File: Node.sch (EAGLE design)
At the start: 53 parts, among them J2 DF12A3.0-14DS, Q1 16MHz, U1 ATMEGA32U4QFN, U2 NRF24L01SMD, U3 LTC3553, U4 L3GD20, U6 LSM303DLHC, U9 RCLAMP0502A, X1 USBSMD

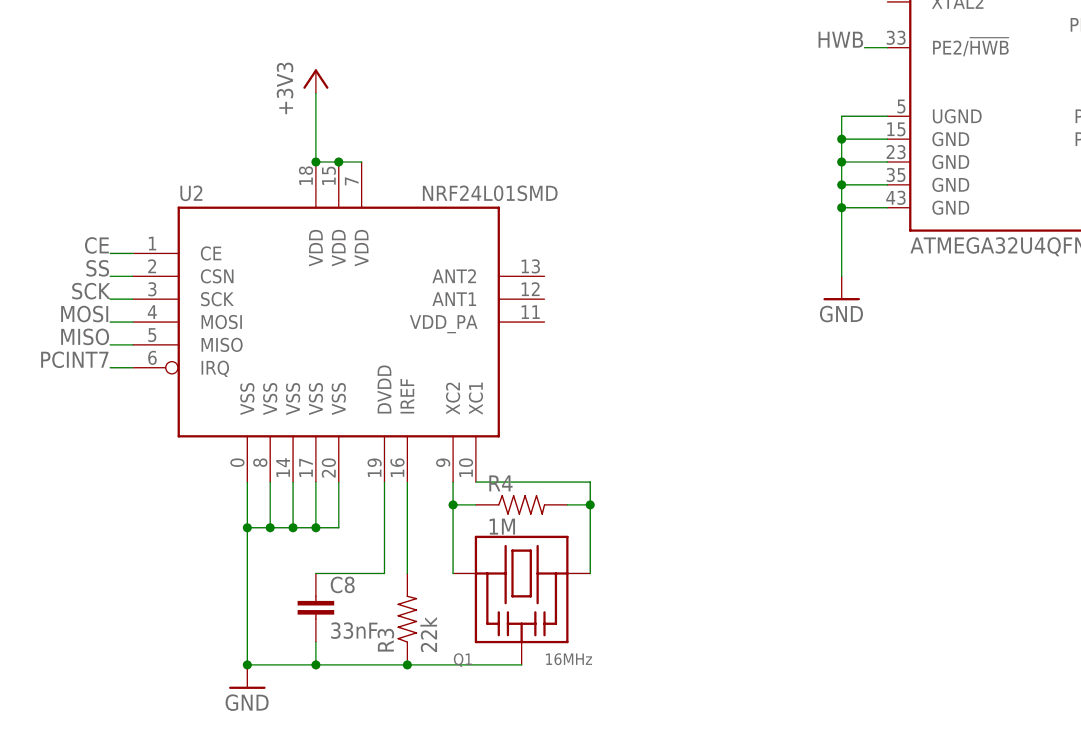
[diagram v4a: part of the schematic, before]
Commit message: balun for nrf24l01
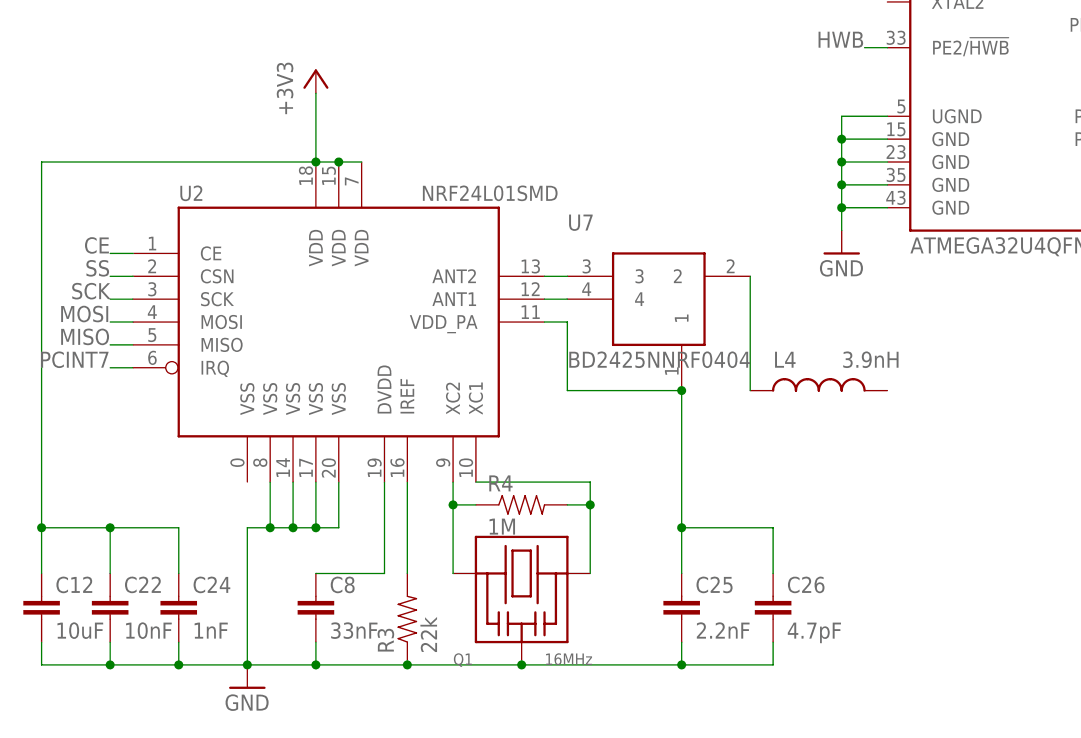
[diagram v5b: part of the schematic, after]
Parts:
- added C12: 10uF, SparkFun:CAP0603-CAP
- added C22: 10nF, SparkFun:CAP0402-CAP
- added C24: 1nF, SparkFun:CAP0402-CAP
- added C25: 2.2nF, SparkFun:CAP0402-CAP
- added C26: 4.7pF, SparkFun:CAP0402-CAP
- added L4: 3.9nH, adjacent-reality:INDUCTOR0402
- added U7: BD2425NNRF0404, adjacent-reality:BD2425NNRF0404
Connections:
- new net N$21: U2.ANT2, U7.3
- new net N$22: U2.ANT1, U7.4
- new net N$23: C25.1, C26.1, U2.VDD_PA, U7.1
- new net N$28: L4.1, U7.2
- net +3V3: now also C12.1, C22.1, C24.1
- net GND: now also C12.2, C22.2, C24.2, C25.2, C26.2; no longer U2.VSS@0
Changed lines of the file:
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@@
 <part name="GND9" library="supply1" deviceset="GND" device=""/>
 <part name="+3V8" library="supply1" deviceset="+3V3" device=""/>
+<part name="C12" library="SparkFun" deviceset="CAP" device="0603-CAP" value="10uF"/>
+<part name="C22" library="SparkFun" deviceset="CAP" device="0402-CAP" value="10nF"/>
+<part name="C24" library="SparkFun" deviceset="CAP" device="0402-CAP" value="1nF"/>
+<part name="C25" library="SparkFun" deviceset="CAP" device="0402-CAP" value="2.2nF"/>
+<part name="C26" library="SparkFun" deviceset="CAP" device="0402-CAP" value="4.7pF"/>
+<part name="L4" library="adjacent-reality" deviceset="INDUCTOR" device="0402" value="3.9nH"/>
+<part name="U7" library="adjacent-reality" deviceset="BD2425NNRF" device="0404"/>
 </parts>
 <sheets>
@@
 <instance part="C7" gate="G$1" x="195.58" y="132.08"/>
 <instance part="GND2" gate="1" x="208.28" y="109.22"/>
-<instance part="GND3" gate="1" x="99.06" y="50.8"/>
+<instance part="GND3" gate="1" x="99.06" y="55.88"/>
 <instance part="+3V3" gate="G$1" x="99.06" y="152.4"/>
 <instance part="X1" gate="G$1" x="20.32" y="187.96" rot="R180"/>
@@
 <instance part="GND9" gate="1" x="185.42" y="121.92"/>
 <instance part="+3V8" gate="G$1" x="185.42" y="149.86"/>
+<instance part="C12" gate="G$1" x="10.16" y="15.24"/>
+<instance part="C22" gate="G$1" x="17.78" y="15.24"/>
+<instance part="C24" gate="G$1" x="25.4" y="15.24"/>
+<instance part="C25" gate="G$1" x="81.28" y="15.24"/>
+<instance part="C26" gate="G$1" x="91.44" y="15.24"/>
+<instance part="L4" gate="G$1" x="96.52" y="40.64" smashed="yes" rot="R90">
+<attribute name="NAME" x="91.44" y="43.18" size="1.778" layer="95"/>
+<attribute name="VALUE" x="99.06" y="43.18" size="1.778" layer="96"/>
+</instance>
+<instance part="U7" gate="G$1" x="78.74" y="50.8"/>
 </instances>
 <busses>
@@
 <wire x1="99.06" y1="60.96" x2="99.06" y2="63.5" width="0.1524" layer="91"/>
 <junction x="99.06" y="63.5"/>
-<wire x1="99.06" y1="60.96" x2="99.06" y2="53.34" width="0.1524" layer="91"/>
+<wire x1="99.06" y1="60.96" x2="99.06" y2="58.42" width="0.1524" layer="91"/>
 <junction x="99.06" y="60.96"/>
 <pinref part="GND3" gate="1" pin="GND"/>
@@
 </segment>
 <segment>
-<pinref part="U2" gate="G$1" pin="VSS@0"/>
 <pinref part="GND4" gate="1" pin="GND"/>
-<wire x1="33.02" y1="30.48" x2="33.02" y2="25.4" width="0.1524" layer="91"/>
 <pinref part="U2" gate="G$1" pin="VSS@8"/>
 <wire x1="33.02" y1="25.4" x2="33.02" y2="10.16" width="0.1524" layer="91"/>
 <wire x1="33.02" y1="25.4" x2="35.56" y2="25.4" width="0.1524" layer="91"/>
 <wire x1="35.56" y1="25.4" x2="35.56" y2="30.48" width="0.1524" layer="91"/>
-<junction x="33.02" y="25.4"/>
 <pinref part="U2" gate="G$1" pin="VSS@14"/>
 <wire x1="35.56" y1="25.4" x2="38.1" y2="25.4" width="0.1524" layer="91"/>
@@
 <wire x1="63.5" y1="10.16" x2="50.8" y2="10.16" width="0.1524" layer="91"/>
 <junction x="50.8" y="10.16"/>
+<pinref part="C12" gate="G$1" pin="2"/>
+<wire x1="10.16" y1="12.7" x2="10.16" y2="10.16" width="0.1524" layer="91"/>
+<wire x1="10.16" y1="10.16" x2="17.78" y2="10.16" width="0.1524" layer="91"/>
+<pinref part="C22" gate="G$1" pin="2"/>
+<wire x1="17.78" y1="10.16" x2="25.4" y2="10.16" width="0.1524" layer="91"/>
+<wire x1="25.4" y1="10.16" x2="33.02" y2="10.16" width="0.1524" layer="91"/>
+<wire x1="17.78" y1="12.7" x2="17.78" y2="10.16" width="0.1524" layer="91"/>
+<junction x="17.78" y="10.16"/>
+<pinref part="C24" gate="G$1" pin="2"/>
+<wire x1="25.4" y1="12.7" x2="25.4" y2="10.16" width="0.1524" layer="91"/>
+<junction x="25.4" y="10.16"/>
+<junction x="63.5" y="10.16"/>
+<pinref part="C25" gate="G$1" pin="2"/>
+<wire x1="81.28" y1="10.16" x2="63.5" y2="10.16" width="0.1524" layer="91"/>
+<wire x1="81.28" y1="12.7" x2="81.28" y2="10.16" width="0.1524" layer="91"/>
+<junction x="81.28" y="10.16"/>
+<pinref part="C26" gate="G$1" pin="2"/>
+<wire x1="91.44" y1="10.16" x2="81.28" y2="10.16" width="0.1524" layer="91"/>
+<wire x1="91.44" y1="12.7" x2="91.44" y2="10.16" width="0.1524" layer="91"/>
 </segment>
 <segment>
@@
 <wire x1="43.18" y1="66.04" x2="45.72" y2="66.04" width="0.1524" layer="91"/>
 <junction x="43.18" y="66.04"/>
+<wire x1="40.64" y1="66.04" x2="10.16" y2="66.04" width="0.1524" layer="91"/>
+<wire x1="10.16" y1="66.04" x2="10.16" y2="25.4" width="0.1524" layer="91"/>
+<wire x1="10.16" y1="25.4" x2="17.78" y2="25.4" width="0.1524" layer="91"/>
+<pinref part="C24" gate="G$1" pin="1"/>
+<wire x1="17.78" y1="25.4" x2="25.4" y2="25.4" width="0.1524" layer="91"/>
+<wire x1="25.4" y1="25.4" x2="25.4" y2="20.32" width="0.1524" layer="91"/>
+<pinref part="C12" gate="G$1" pin="1"/>
+<wire x1="10.16" y1="25.4" x2="10.16" y2="20.32" width="0.1524" layer="91"/>
+<junction x="10.16" y="25.4"/>
+<pinref part="C22" gate="G$1" pin="1"/>
+<wire x1="17.78" y1="25.4" x2="17.78" y2="20.32" width="0.1524" layer="91"/>
+<junction x="17.78" y="25.4"/>
 </segment>
 <segment>
@@
 </segment>
 </net>
+<net name="N$21" class="0">
+<segment>
+<pinref part="U2" gate="G$1" pin="ANT2"/>
+<pinref part="U7" gate="G$1" pin="3"/>
+<wire x1="66.04" y1="53.34" x2="68.58" y2="53.34" width="0.1524" layer="91"/>
+</segment>
+</net>
+<net name="N$22" class="0">
+<segment>
+<pinref part="U2" gate="G$1" pin="ANT1"/>
+<pinref part="U7" gate="G$1" pin="4"/>
+<wire x1="66.04" y1="50.8" x2="68.58" y2="50.8" width="0.1524" layer="91"/>
+</segment>
+</net>
+<net name="N$23" class="0">
+<segment>
+<pinref part="C25" gate="G$1" pin="1"/>
+<pinref part="C26" gate="G$1" pin="1"/>
+<wire x1="91.44" y1="25.4" x2="91.44" y2="20.32" width="0.1524" layer="91"/>
+<wire x1="81.28" y1="25.4" x2="91.44" y2="25.4" width="0.1524" layer="91"/>
+<wire x1="81.28" y1="25.4" x2="81.28" y2="20.32" width="0.1524" layer="91"/>
+<pinref part="U2" gate="G$1" pin="VDD_PA"/>
+<wire x1="66.04" y1="48.26" x2="68.58" y2="48.26" width="0.1524" layer="91"/>
+<wire x1="68.58" y1="48.26" x2="68.58" y2="40.64" width="0.1524" layer="91"/>
+<pinref part="U7" gate="G$1" pin="1"/>
+<wire x1="68.58" y1="40.64" x2="81.28" y2="40.64" width="0.1524" layer="91"/>
+<wire x1="81.28" y1="25.4" x2="81.28" y2="40.64" width="0.1524" layer="91"/>
+<junction x="81.28" y="25.4"/>
+<junction x="81.28" y="40.64"/>
+</segment>
+</net>
+<net name="N$28" class="0">
+<segment>
+<pinref part="U7" gate="G$1" pin="2"/>
+<pinref part="L4" gate="G$1" pin="1"/>
+<wire x1="88.9" y1="53.34" x2="88.9" y2="40.64" width="0.1524" layer="91"/>
+</segment>
+</net>
